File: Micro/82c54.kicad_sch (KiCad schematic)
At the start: 7 parts, among them U14 82C54_PLCC, U16 74HC32, U32 74HC08, U33 74HC04, U49 74HC08

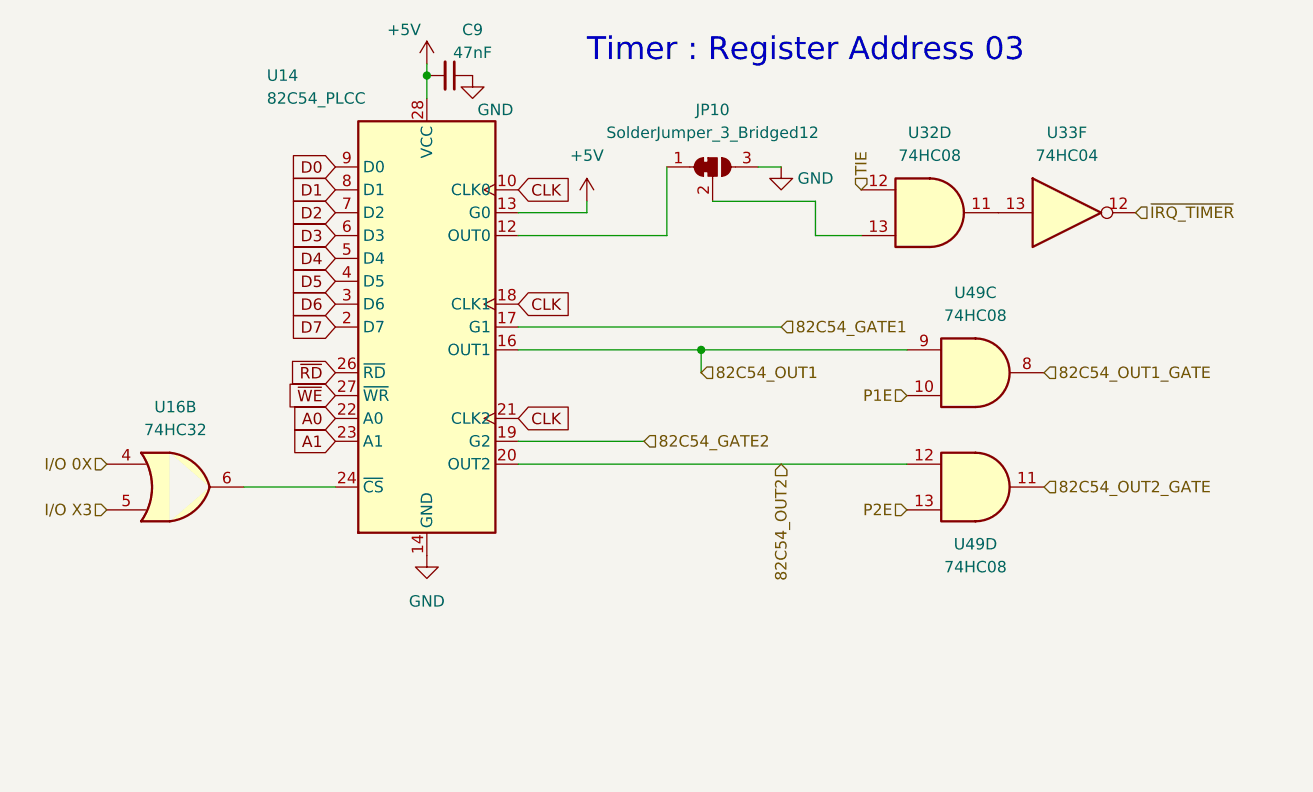
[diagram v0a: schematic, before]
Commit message: Hardware: fixed error in schematic with clock moved dotclock to out 2 (better for jitter) allowed the replacement of 82c54 CPU CLK with CLK 2 moved nmi switch to a more reasonable location
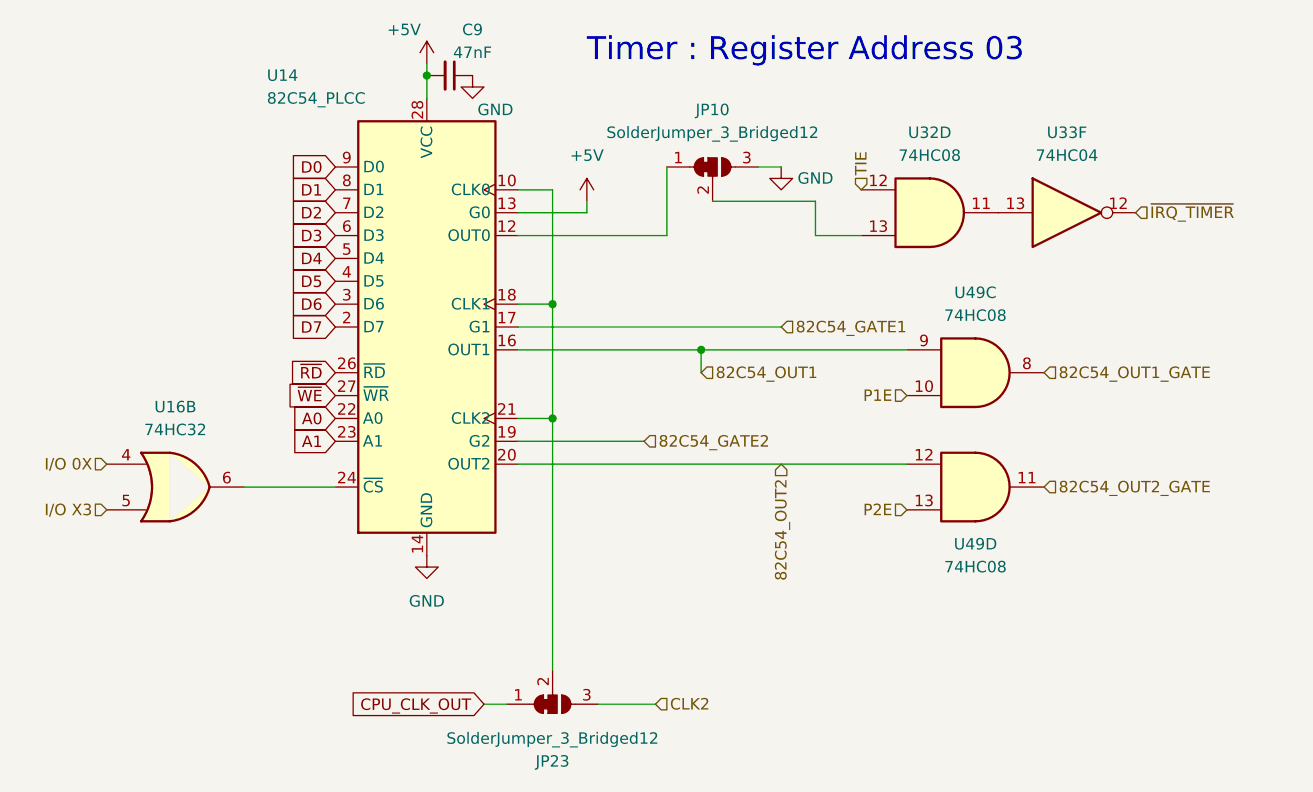
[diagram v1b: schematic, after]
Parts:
- added JP23: SolderJumper_3_Bridged12, Jumper:SolderJumper-3_P1.3mm_Bridged12_RoundedPad1.0x1.5mm_NumberLabels, symbol Jumper:SolderJumper_3_Bridged12
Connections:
- net CLK: no longer names the net of U14.10 (CLK0), U14.18 (CLK1), U14.21 (CLK2)
- net CLK: now also JP23.2 (C)
- new net CLK2: JP23.3 (B)
- new net CPU_CLK_OUT: JP23.1 (A)
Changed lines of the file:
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@@
   (junction (at 58.42 19.05) (diameter 0) (color 0 0 0 0)
   )
+  (junction (at 72.39 57.15) (diameter 0) (color 0 0 0 0)
+  )
+  (junction (at 72.39 44.45) (diameter 0) (color 0 0 0 0)
+  )
   (junction (at 88.9 49.53) (diameter 0) (color 0 0 0 0)
   )
@@
     (stroke (width 0) (type default))
   )
+  (wire (pts (xy 72.39 31.75) (xy 72.39 44.45))
+    (stroke (width 0) (type default))
+  )
   (wire (pts (xy 97.79 29.21) (xy 95.25 29.21))
     (stroke (width 0) (type default))
   )
+  (wire (pts (xy 68.58 44.45) (xy 72.39 44.45))
+    (stroke (width 0) (type default))
+  )
   (wire (pts (xy 76.2 34.29) (xy 76.2 33.02))
     (stroke (width 0) (type default))
@@
     (stroke (width 0) (type default))
   )
+  (wire (pts (xy 72.39 57.15) (xy 68.58 57.15))
+    (stroke (width 0) (type default))
+  )
+  (wire (pts (xy 72.39 44.45) (xy 72.39 57.15))
+    (stroke (width 0) (type default))
+  )
   (wire (pts (xy 68.58 36.83) (xy 85.09 36.83))
     (stroke (width 0) (type default))
@@
     (stroke (width 0) (type default))
   )
+  (wire (pts (xy 72.39 85.09) (xy 72.39 57.15))
+    (stroke (width 0) (type default))
+  )
   (wire (pts (xy 68.58 34.29) (xy 76.2 34.29))
     (stroke (width 0) (type default))
@@
     (stroke (width 0) (type default))
   )
+  (wire (pts (xy 68.58 31.75) (xy 72.39 31.75))
+    (stroke (width 0) (type default))
+  )
+  (wire (pts (xy 67.31 88.9) (xy 64.77 88.9))
+    (stroke (width 0) (type default))
+  )
   (wire (pts (xy 101.6 36.83) (xy 106.68 36.83))
     (stroke (width 0) (type default))
   )
   (wire (pts (xy 68.58 62.23) (xy 111.76 62.23))
+    (stroke (width 0) (type default))
+  )
+  (wire (pts (xy 83.82 88.9) (xy 77.47 88.9))
     (stroke (width 0) (type default))
   )
@@
     )
   )
+  (global_label "CPU_CLK_OUT" (shape input) (at 64.77 88.9 180) (fields_autoplaced)
+    (effects (font (size 1.27 1.27)) (justify right))
+    (property "Intersheetrefs" "${INTERSHEET_REFS}" (at 48.7824 88.9 0)
+      (effects (font (size 1.27 1.27)) (justify right) hide)
+    )
+  )
   (global_label "D1" (shape input) (at 48.26 31.75 180) (fields_autoplaced)
     (effects (font (size 1.27 1.27)) (justify right))
@@
     )
   )
-  (global_label "CLK" (shape input) (at 68.58 57.15 0) (fields_autoplaced)
-    (effects (font (size 1.27 1.27)) (justify left))
-    (property "Intersheetrefs" "${INTERSHEET_REFS}" (at 75.1333 57.15 0)
-      (effects (font (size 1.27 1.27)) (justify left) hide)
-    )
-  )
   (global_label "D7" (shape input) (at 48.26 46.99 180) (fields_autoplaced)
     (effects (font (size 1.27 1.27)) (justify right))
@@
     )
   )
-  (global_label "CLK" (shape input) (at 68.58 44.45 0) (fields_autoplaced)
-    (effects (font (size 1.27 1.27)) (justify left))
-    (property "Intersheetrefs" "${INTERSHEET_REFS}" (at 75.1333 44.45 0)
-      (effects (font (size 1.27 1.27)) (justify left) hide)
-    )
-  )
   (global_label "~{WE}" (shape input) (at 48.26 54.61 180) (fields_autoplaced)
     (effects (font (size 1.27 1.27)) (justify right))
@@
     )
   )
-  (global_label "CLK" (shape input) (at 68.58 31.75 0) (fields_autoplaced)
-    (effects (font (size 1.27 1.27)) (justify left))
-    (property "Intersheetrefs" "${INTERSHEET_REFS}" (at 75.1333 31.75 0)
-      (effects (font (size 1.27 1.27)) (justify left) hide)
-    )
-  )
   (global_label "D2" (shape input) (at 48.26 34.29 180) (fields_autoplaced)
     (effects (font (size 1.27 1.27)) (justify right))
@@
   )
   (hierarchical_label "82C54_OUT2_GATE" (shape input) (at 127 64.77 0) (fields_autoplaced)
+    (effects (font (size 1.27 1.27)) (justify left))
+  )
+  (hierarchical_label "CLK2" (shape input) (at 83.82 88.9 0) (fields_autoplaced)
     (effects (font (size 1.27 1.27)) (justify left))
   )
@@
         )
       )
+    )
+  )
+  (symbol (lib_id "Jumper:SolderJumper_3_Bridged12") (at 72.39 88.9 0) (mirror x) (unit 1)
+    (in_bom yes) (on_board yes) (dnp no) (fields_autoplaced)
+    (property "Reference" "JP23" (at 72.39 95.25 0)
+      (effects (font (size 1.27 1.27)))
+    )
+    (property "Value" "SolderJumper_3_Bridged12" (at 72.39 92.71 0)
+      (effects (font (size 1.27 1.27)))
+    )
+    (property "Footprint" "Jumper:SolderJumper-3_P1.3mm_Bridged12_RoundedPad1.0x1.5mm_NumberLabels" (at 72.39 88.9 0)
+      (effects (font (size 1.27 1.27)) hide)
+    )
+    (property "Datasheet" "~" (at 72.39 88.9 0)
+      (effects (font (size 1.27 1.27)) hide)
+    )
+    (pin "1")
+    (pin "2")
+    (pin "3")
+    (instances
+      (project "Micro"
+        (path "/5388c84f-02a4-4503-bb12-5559371e0a41/60bf3c7c-7133-4ca1-aa44-3c0fc6d461d6"
+          (reference "JP23") (unit 1)
+        )
+        (path "/5388c84f-02a4-4503-bb12-5559371e0a41/df04dcad-608f-4a5f-9459-edcdeb427672/169ad534-9a83-4c27-91bb-a66bdb2b31fe"
+          (reference "JP24") (unit 1)
+        )
+      )
